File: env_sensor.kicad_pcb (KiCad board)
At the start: 2 copper layers, 88 x 73 mm, 232 parts, among them J1 E Paper, J10 PWMOUT, J11 Reg2, J13 Conn_01x03_Socket, J15 MH-Z19, J16 ADCs, J17 Conn_01x04_Pin, J18 Conn_01x02_Pin, J2 Reg1, J3 Barrel_Jack, J4 LED_OUTPUT, J5 Conn_01x04_Pin, J6 Conn_01x08_Socket, J7 USB_C_Receptacle_USB2.0_16P, J8 Conn_01x08_Pin, J9 DEBUG, Q1 NMOS, Q2 NMOS, Q3 NMOS, SW1 EN, SW2 BOOT, U1 MH-Z19B, U3 ESP32-S3-WROOM-1, U4 TXB0104PW, U6 TPS2065CDBV, U7 AP7361C-33E, Y1 Crystal

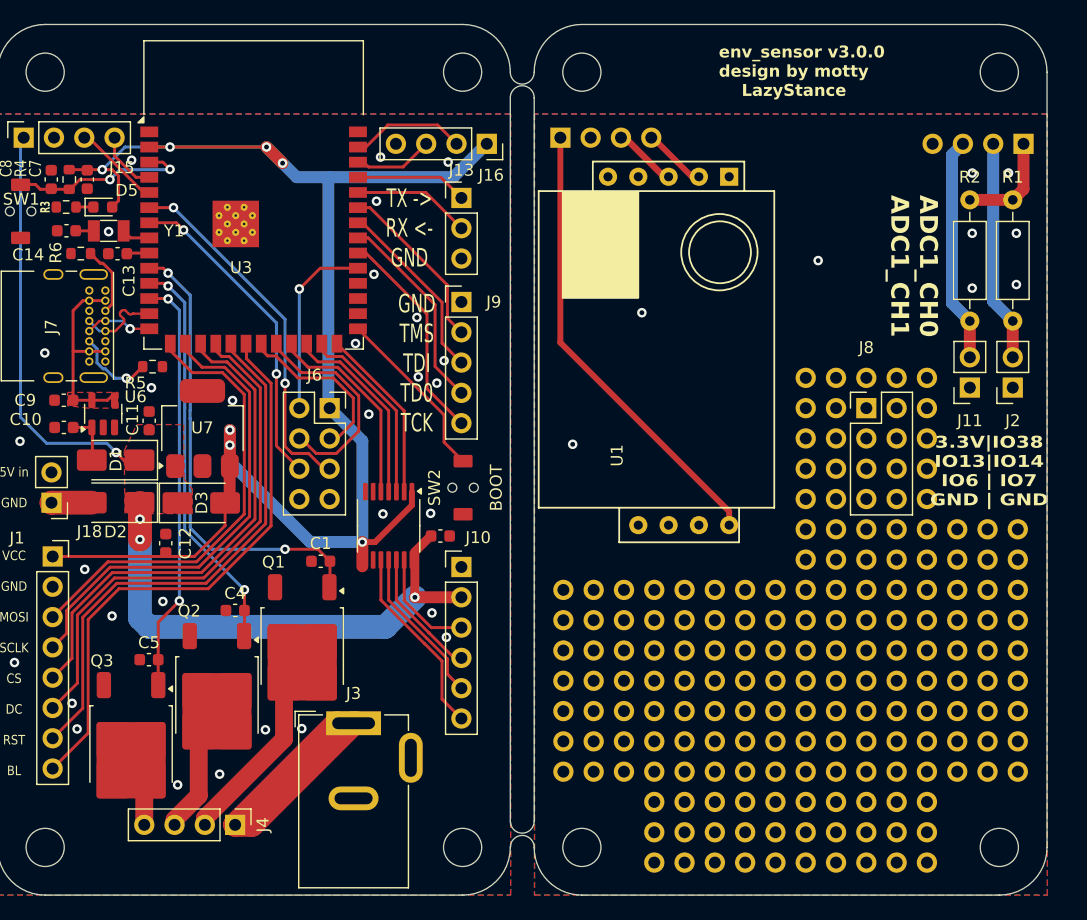
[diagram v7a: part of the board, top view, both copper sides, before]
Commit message: delete extension board
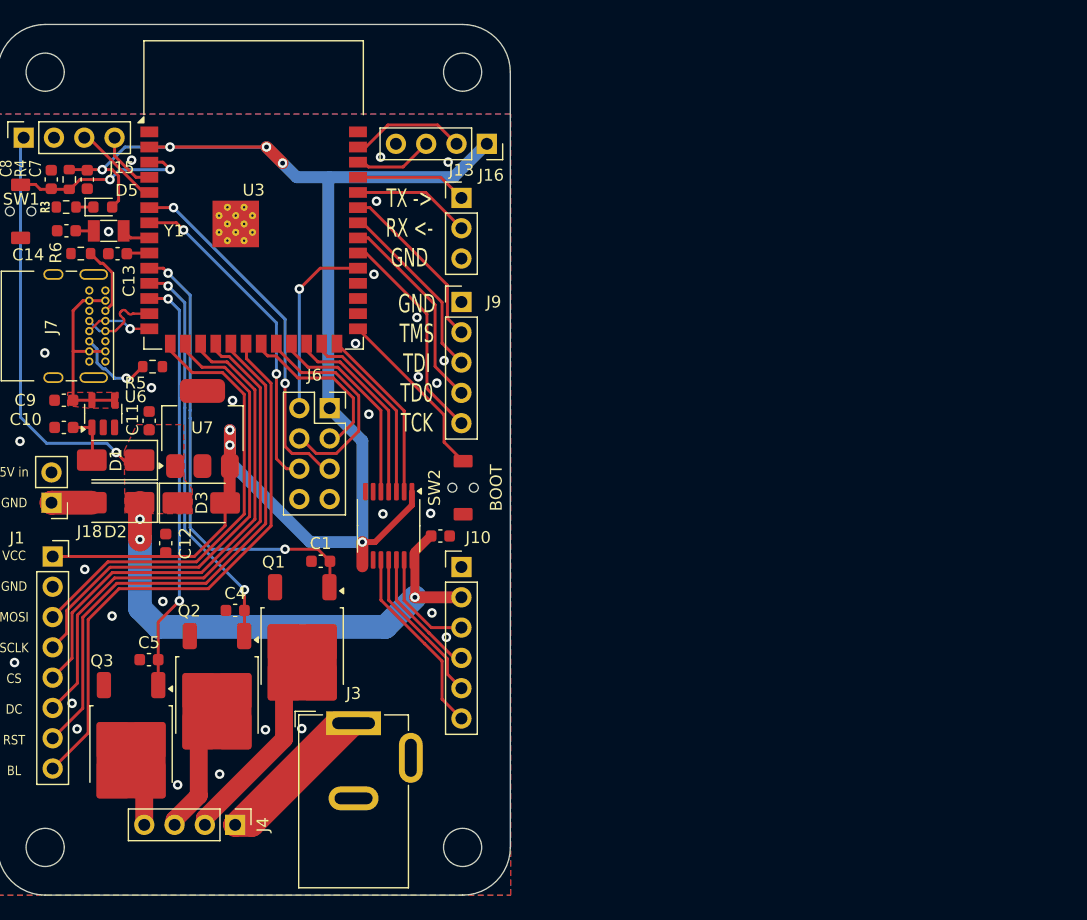
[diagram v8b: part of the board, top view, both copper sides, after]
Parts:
- removed ? (x165): ThroughHole1x01_P2.54mm, env-sensor:ThroughHole1x01_P2.54mm
- removed ? (x10): , 
- removed J11: Reg2, Connector_PinSocket_2.54mm:PinSocket_1x02_P2.54mm_Vertical
- removed J17, J5: Conn_01x04_Pin, Connector_PinHeader_2.54mm:PinHeader_1x04_P2.54mm_Vertical
- removed J2: Reg1, Connector_PinSocket_2.54mm:PinSocket_1x02_P2.54mm_Vertical
- removed J8: Conn_01x08_Pin, Connector_PinHeader_2.54mm:PinHeader_2x04_P2.54mm_Vertical
- removed R1, R2: ~, Resistor_THT:R_Axial_DIN0207_L6.3mm_D2.5mm_P10.16mm_Horizontal
- removed the REF** at (149.0, 45.0)
- removed the REF** at (184.0, 45.0)
- removed the REF** at (184.0, 110.0)
- removed the REF** at (149.0, 110.0)
- removed U1: MH-Z19B, mh-z19b:Winsen_MH-Z19B
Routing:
- net /sensor/v5v: track 38.3 -> 0.00 mm
- net /sensor/adc2: track 18.9 -> 0.00 mm
- net /sensor/adc1: track 18.6 -> 0.00 mm
- net /sensor/adc_v3v: track 9.05 -> 0.00 mm
- net /sensor/TX(ESP_DOWN): track 5.35 -> 0.00 mm
- net /sensor/RX(ESP_UP): track 5.35 -> 0.00 mm
- net IO7: track 27.1 -> 27.8 mm
- net /sensor/GND: vias 9 -> 0
- removed copper zone on B.Cu, net /sensor/GND
- removed copper zone on F.Cu, net /sensor/GND
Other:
- board size 88 x 73 mm -> 43 x 73 mm
- board text removed: "3.3V|IO38 IO13|IO14 IO6 | IO7 GND | GND"
- board text removed: "ADC1_CH0 ADC1_CH1"
